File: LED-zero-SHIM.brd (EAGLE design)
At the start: 30 x 65 mm, 157 parts, among them IC1 TXB0101DCKR

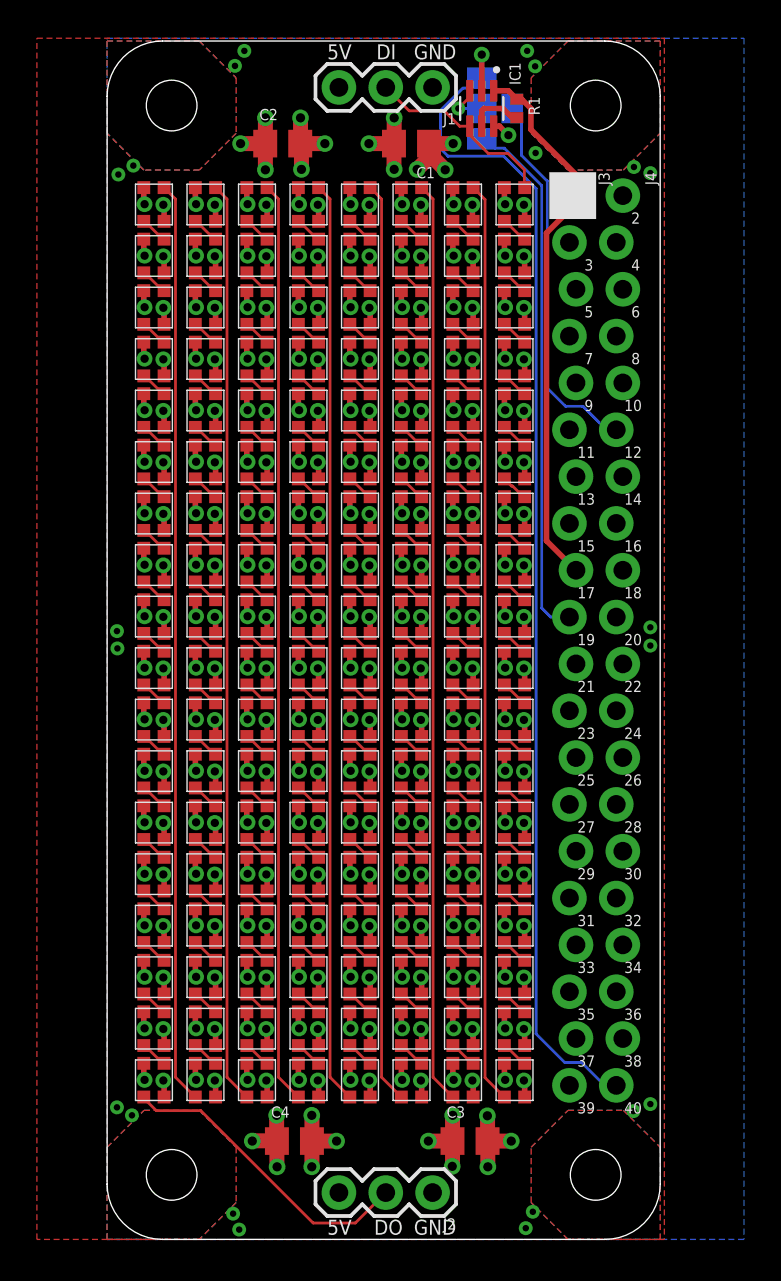
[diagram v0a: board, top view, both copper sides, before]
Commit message: Moved some traces and vias around
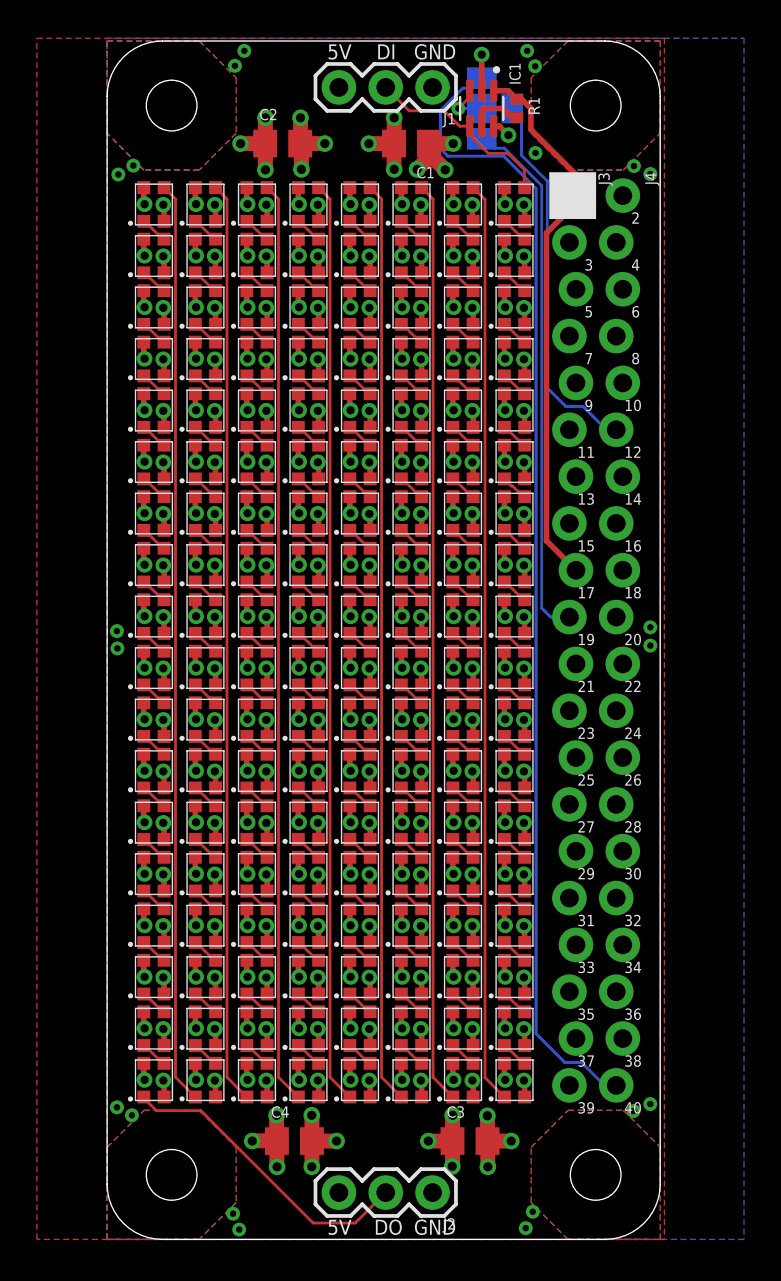
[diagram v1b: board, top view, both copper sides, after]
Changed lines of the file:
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@@
 <drawing>
 <settings>
-<setting alwaysvectorfont="yes"/>
+<setting alwaysvectorfont="no"/>
 <setting verticaltext="up"/>
 </settings>
@@
 <contactref element="J3" pad="13"/>
 <contactref element="J3" pad="20"/>
-<polygon width="0.1524" layer="16" isolate="0.254">
+<polygon width="0.1524" layer="16" isolate="0.254" thermals="no">
 <vertex x="0" y="0"/>
 <vertex x="0" y="65.151"/>
@@
 <wire x1="8.678" y1="8.5784" x2="8.636" y2="8.6204" width="0.3048" layer="1"/>
 <via x="8.636" y="8.6204" extent="1-16" drill="0.45"/>
-<polygon width="0.1524" layer="2" isolate="0.254">
+<polygon width="0.1524" layer="2" isolate="0.254" thermals="no">
 <vertex x="0" y="0"/>
 <vertex x="30.226" y="0"/>
@@
 <via x="0.6096" y="57.7596" extent="1-16" drill="0.35"/>
 <via x="23.2156" y="63.627" extent="1-16" drill="0.35"/>
-<via x="28.575" y="58.166" extent="1-16" drill="0.35"/>
+<via x="29.464" y="57.785" extent="1-16" drill="0.35"/>
 <via x="28.5496" y="6.9596" extent="1-16" drill="0.35"/>
 <via x="23.0886" y="1.4986" extent="1-16" drill="0.35"/>
@@
 <wire x1="7.578" y1="8.6936" x2="7.62" y2="8.6516" width="0.3048" layer="1"/>
 <via x="7.62" y="8.6516" extent="1-16" drill="0.45"/>
-<polygon width="0.1524" layer="15" isolate="0.254">
+<polygon width="0.1524" layer="15" isolate="0.254" thermals="no">
 <vertex x="0" y="-3.81"/>
 <vertex x="0" y="65.151"/>
@@
 <vertex x="30.226" y="-3.81"/>
 </polygon>
-<polygon width="0.1524" layer="1">
+<polygon width="0.1524" layer="1" thermals="no">
 <vertex x="30.226" y="0"/>
 <vertex x="-3.81" y="0"/>
@@
 <via x="18.7198" y="3.9624" extent="1-16" drill="0.5"/>
 <via x="22.7838" y="64.4652" extent="1-16" drill="0.35"/>
-<via x="29.464" y="57.8358" extent="1-16" drill="0.35"/>
+<via x="28.575" y="58.2168" extent="1-16" drill="0.35"/>
 <via x="7.4422" y="64.4652" extent="1-16" drill="0.35"/>
 <via x="1.4224" y="58.2422" extent="1-16" drill="0.35"/>
